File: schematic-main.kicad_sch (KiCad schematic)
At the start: 9 parts, among them J1 Conn_01x02_Pin, J2 Conn_01x02_Pin, J3 Conn_01x02_Pin, J4 Conn_01x02_Pin, P1 USB_C_Plug_USB2.0

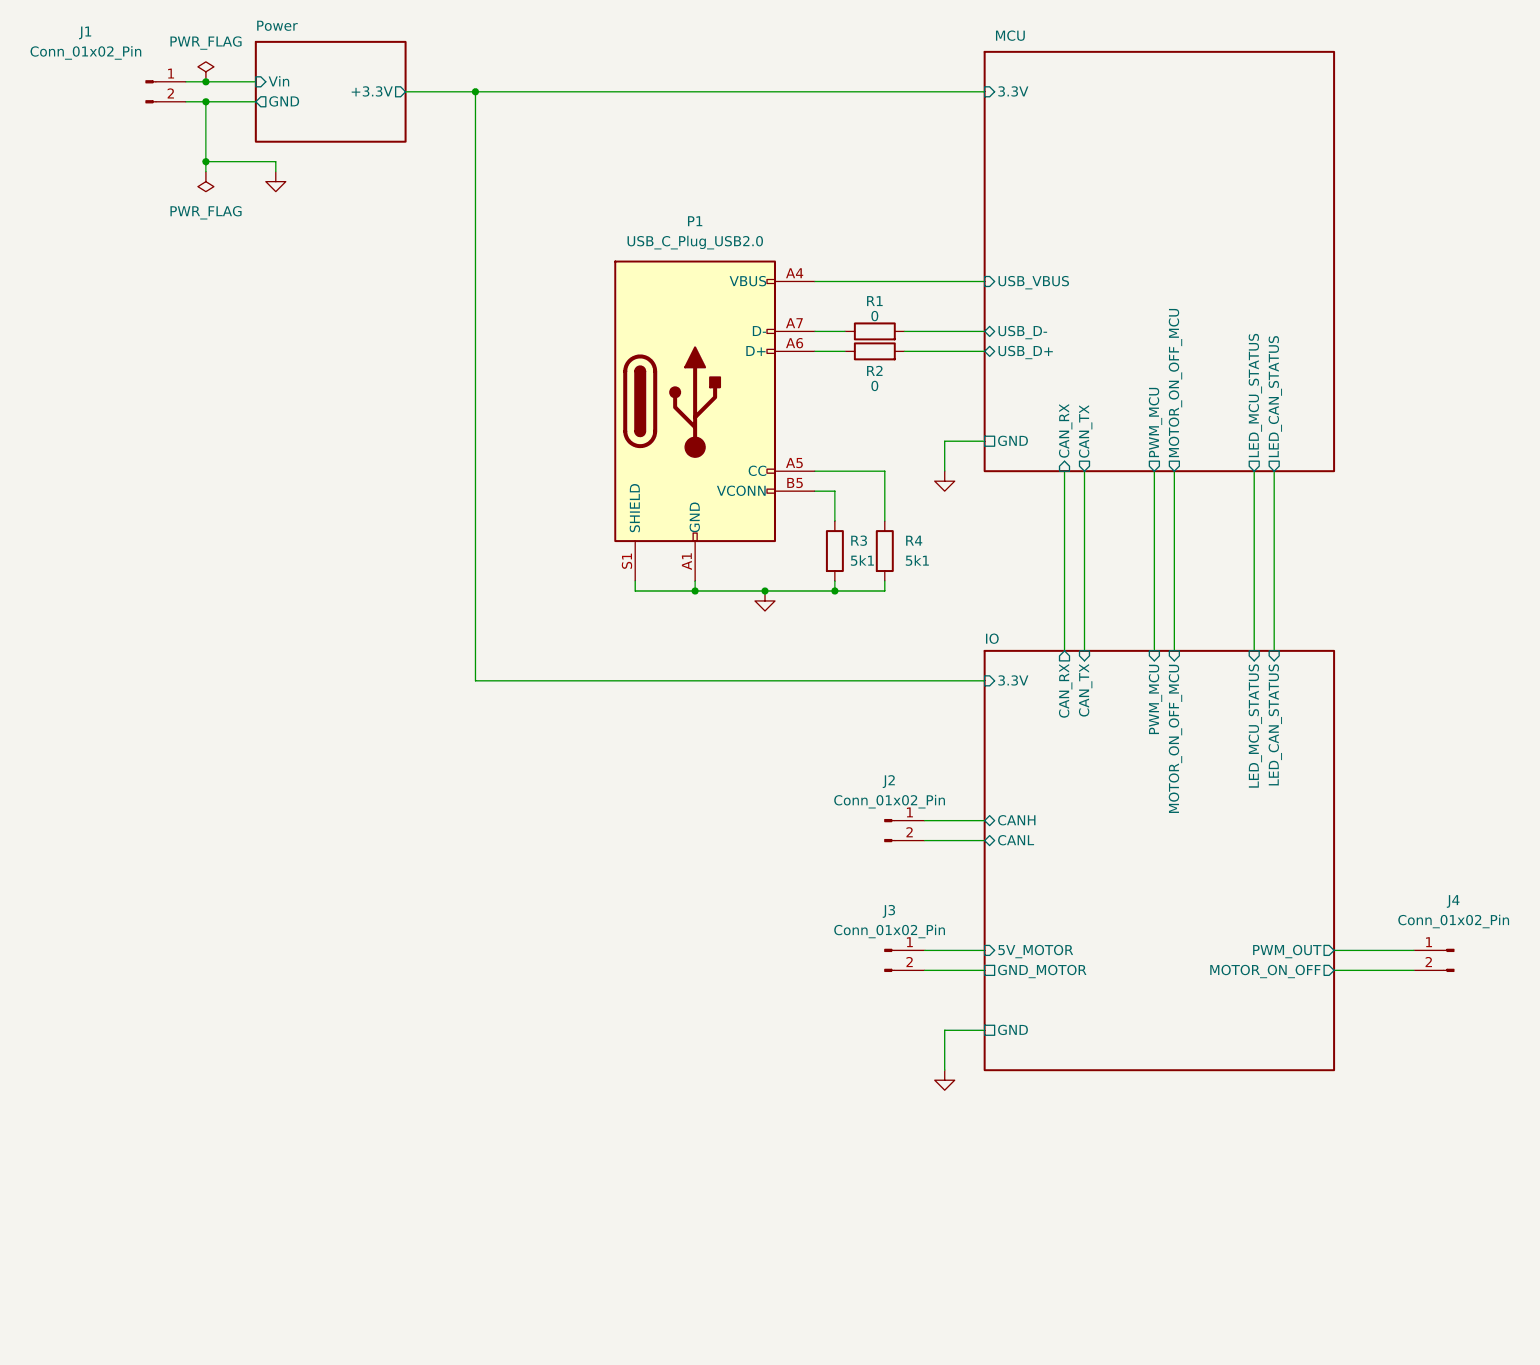
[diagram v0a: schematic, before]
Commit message: Add values for ideal diode circuit
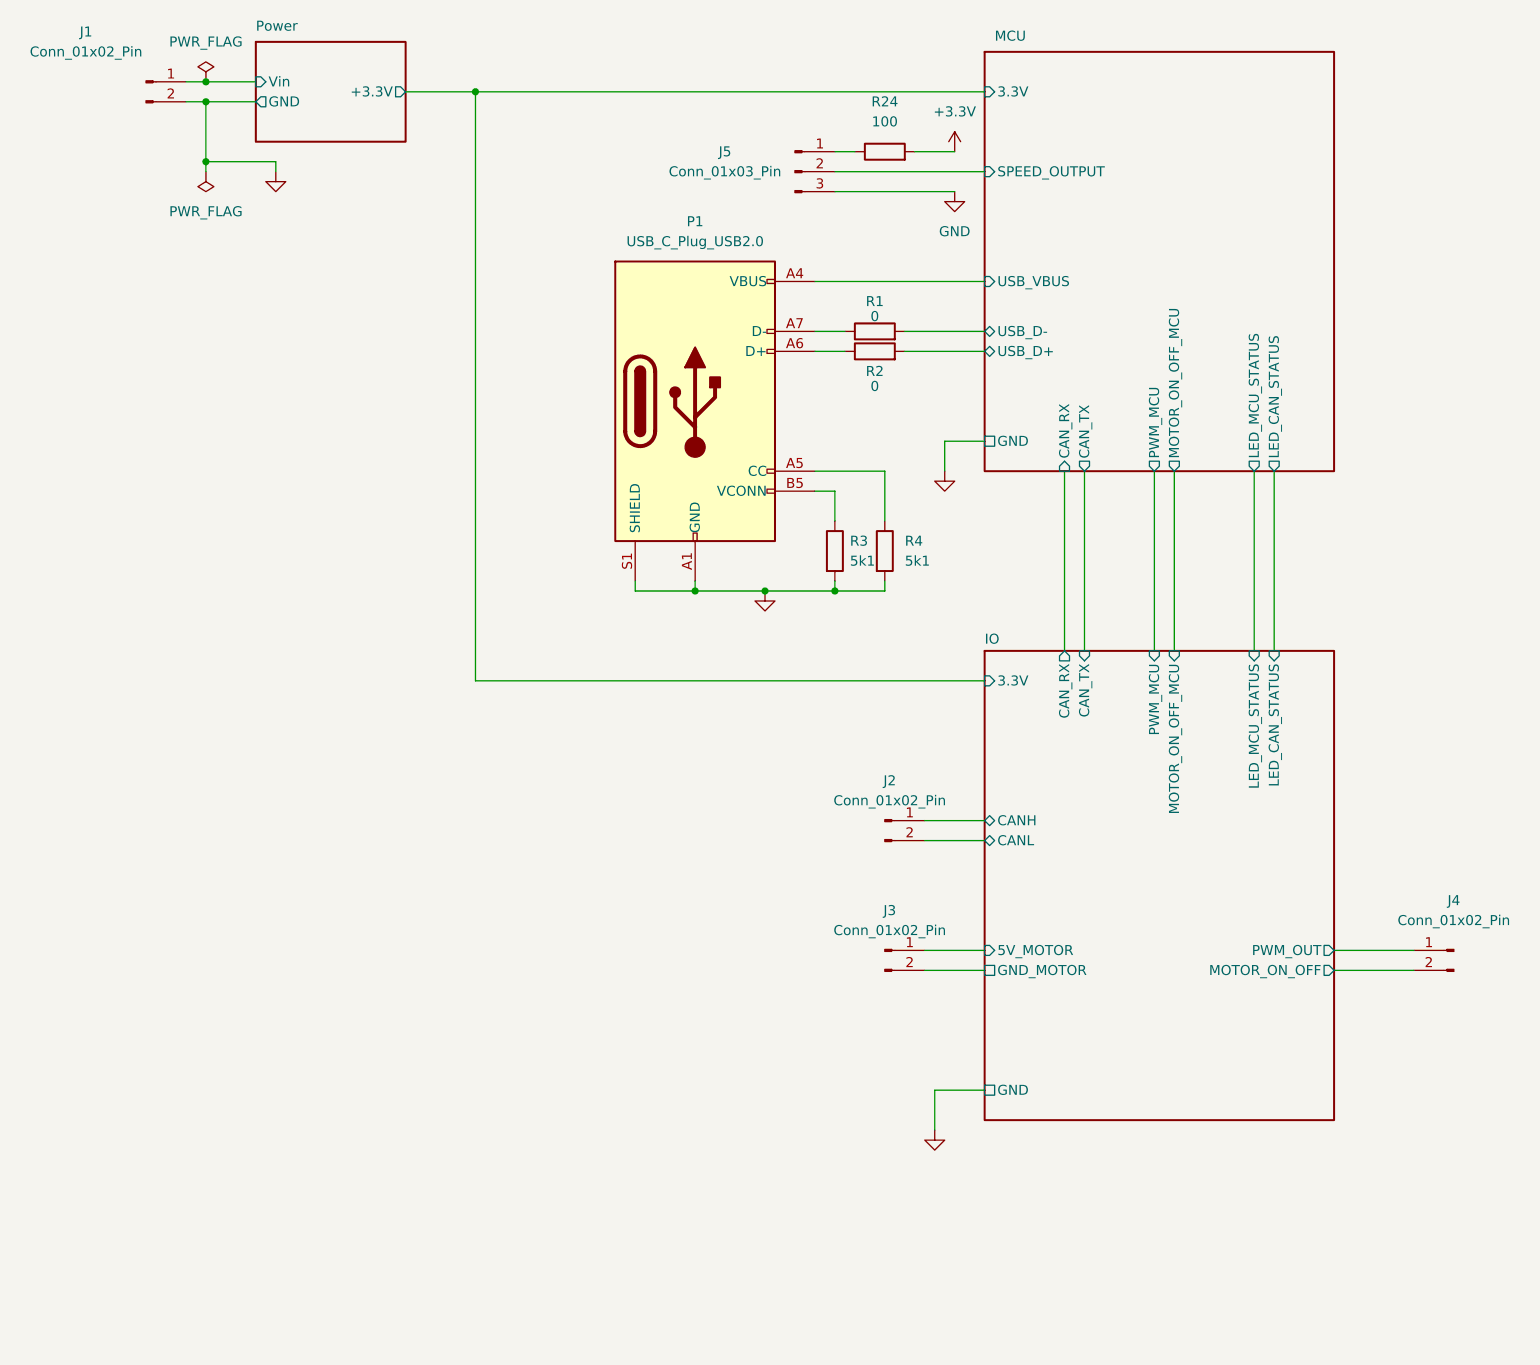
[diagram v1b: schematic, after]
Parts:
- added J5: Conn_01x03_Pin, symbol Connector:Conn_01x03_Pin
- added R24: 100, symbol Device:R
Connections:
- net GND: now also J5.3 (Pin_3)
- new net: J5.1 (Pin_1), R24.1
- new net +3.3V: R24.2
- new net MCU/SPEED_OUTPUT: J5.2 (Pin_2)
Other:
- sheet MCU ports: added SPEED_OUTPUT; removed none
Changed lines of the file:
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@@
+    (stroke (width 0) (type default))
+  )
+  (wire (pts (xy 115.57 40.64) (xy 118.11 40.64))
     (stroke (width 0) (type default))
   )
@@
     (stroke (width 0) (type default))
   )
+  (wire (pts (xy 115.57 45.72) (xy 130.81 45.72))
+    (stroke (width 0) (type default))
+  )
   (wire (pts (xy 156.21 81.28) (xy 156.21 104.14))
     (stroke (width 0) (type default))
@@
     (stroke (width 0) (type default))
   )
+  (wire (pts (xy 115.57 43.18) (xy 134.62 43.18))
+    (stroke (width 0) (type default))
+  )
+  (wire (pts (xy 125.73 40.64) (xy 130.81 40.64))
+    (stroke (width 0) (type default))
+  )
   (wire (pts (xy 69.85 33.02) (xy 69.85 107.95))
     (stroke (width 0) (type default))
@@
     (stroke (width 0) (type default))
   )
-  (wire (pts (xy 134.62 152.4) (xy 129.54 152.4))
+  (wire (pts (xy 134.62 160.02) (xy 128.27 160.02))
     (stroke (width 0) (type default))
   )
@@
     (stroke (width 0) (type default))
   )
-  (wire (pts (xy 129.54 152.4) (xy 129.54 157.48))
+  (wire (pts (xy 128.27 160.02) (xy 128.27 165.1))
     (stroke (width 0) (type default))
   )
@@
     (stroke (width 0) (type default))
   )
-  (symbol (lib_id "power:GND") (at 129.54 157.48 0) (unit 1)
-    (in_bom yes) (on_board yes) (dnp no) (fields_autoplaced)
-    (property "Reference" "#PWR04" (at 129.54 163.83 0)
-      (effects (font (size 1.27 1.27)) hide)
-    )
-    (property "Value" "GND" (at 129.54 162.56 0)
-      (effects (font (size 1.27 1.27)) hide)
-    )
-    (property "Footprint" "" (at 129.54 157.48 0)
-      (effects (font (size 1.27 1.27)) hide)
-    )
-    (property "Datasheet" "" (at 129.54 157.48 0)
+  (symbol (lib_id "power:GND") (at 128.27 165.1 0) (unit 1)
+    (in_bom yes) (on_board yes) (dnp no) (fields_autoplaced)
+    (property "Reference" "#PWR04" (at 128.27 171.45 0)
+      (effects (font (size 1.27 1.27)) hide)
+    )
+    (property "Value" "GND" (at 128.27 170.18 0)
+      (effects (font (size 1.27 1.27)) hide)
+    )
+    (property "Footprint" "" (at 128.27 165.1 0)
+      (effects (font (size 1.27 1.27)) hide)
+    )
+    (property "Datasheet" "" (at 128.27 165.1 0)
       (effects (font (size 1.27 1.27)) hide)
     )
@@
     )
   )
+  (symbol (lib_id "power:+3.3V") (at 130.81 40.64 0) (unit 1)
+    (in_bom yes) (on_board yes) (dnp no) (fields_autoplaced)
+    (property "Reference" "#PWR052" (at 130.81 44.45 0)
+      (effects (font (size 1.27 1.27)) hide)
+    )
+    (property "Value" "+3.3V" (at 130.81 35.56 0)
+      (effects (font (size 1.27 1.27)))
+    )
+    (property "Footprint" "" (at 130.81 40.64 0)
+      (effects (font (size 1.27 1.27)) hide)
+    )
+    (property "Datasheet" "" (at 130.81 40.64 0)
+      (effects (font (size 1.27 1.27)) hide)
+    )
+    (pin "1")
+    (instances
+      (project "schematic-main"
+        (path "/c9ad7189-d3b2-414a-9743-efd8e57cd755"
+          (reference "#PWR052") (unit 1)
+        )
+      )
+    )
+  )
   (symbol (lib_id "power:GND") (at 44.45 43.18 0) (unit 1)
     (in_bom yes) (on_board yes) (dnp no) (fields_autoplaced)
@@
       (effects (font (size 1.27 1.27)) hide)
     )
-    (pin "2")
-    (pin "1")
+    (pin "1")
+    (pin "2")
     (instances
       (project "schematic-main"
@@
     )
   )
+  (symbol (lib_id "Device:R") (at 121.92 40.64 90) (unit 1)
+    (in_bom yes) (on_board yes) (dnp no) (fields_autoplaced)
+    (property "Reference" "R24" (at 121.92 34.29 90)
+      (effects (font (size 1.27 1.27)))
+    )
+    (property "Value" "100" (at 121.92 36.83 90)
+      (effects (font (size 1.27 1.27)))
+    )
+    (property "Footprint" "" (at 121.92 42.418 90)
+      (effects (font (size 1.27 1.27)) hide)
+    )
+    (property "Datasheet" "~" (at 121.92 40.64 0)
+      (effects (font (size 1.27 1.27)) hide)
+    )
+    (pin "1")
+    (pin "2")
+    (instances
+      (project "schematic-main"
+        (path "/c9ad7189-d3b2-414a-9743-efd8e57cd755"
+          (reference "R24") (unit 1)
+        )
+      )
+    )
+  )
   (symbol (lib_id "power:GND") (at 129.54 81.28 0) (unit 1)
     (in_bom yes) (on_board yes) (dnp no) (fields_autoplaced)
@@
       (effects (font (size 1.27 1.27)) hide)
     )
-    (pin "2")
-    (pin "1")
+    (pin "1")
+    (pin "2")
     (instances
       (project "schematic-main"
@@
     )
   )
+  (symbol (lib_id "Connector:Conn_01x03_Pin") (at 110.49 43.18 0) (unit 1)
+    (in_bom yes) (on_board yes) (dnp no)
+    (property "Reference" "J5" (at 101.6 40.64 0)
+      (effects (font (size 1.27 1.27)))
+    )
+    (property "Value" "Conn_01x03_Pin" (at 101.6 43.18 0)
+      (effects (font (size 1.27 1.27)))
+    )
+    (property "Footprint" "" (at 110.49 43.18 0)
+      (effects (font (size 1.27 1.27)) hide)
+    )
+    (property "Datasheet" "~" (at 110.49 43.18 0)
+      (effects (font (size 1.27 1.27)) hide)
+    )
+    (pin "1")
+    (pin "2")
+    (pin "3")
+    (instances
+      (project "schematic-main"
+        (path "/c9ad7189-d3b2-414a-9743-efd8e57cd755"
+          (reference "J5") (unit 1)
+        )
+      )
+    )
+  )
   (symbol (lib_id "power:GND") (at 106.68 96.52 0) (unit 1)
     (in_bom yes) (on_board yes) (dnp no) (fields_autoplaced)
@@
       (effects (font (size 1.27 1.27)) hide)
     )
-    (pin "2")
-    (pin "1")
+    (pin "1")
+    (pin "2")
     (instances
       (project "schematic-main"
@@
       (effects (font (size 1.27 1.27)) hide)
     )
-    (pin "2")
-    (pin "1")
+    (pin "1")
+    (pin "2")
     (instances
       (project "schematic-main"
         (path "/c9ad7189-d3b2-414a-9743-efd8e57cd755"
           (reference "J4") (unit 1)
+        )
+      )
+    )
+  )
+  (symbol (lib_id "power:GND") (at 130.81 45.72 0) (unit 1)
+    (in_bom yes) (on_board yes) (dnp no) (fields_autoplaced)
+    (property "Reference" "#PWR053" (at 130.81 52.07 0)
+      (effects (font (size 1.27 1.27)) hide)
+    )
+    (property "Value" "GND" (at 130.81 50.8 0)
+      (effects (font (size 1.27 1.27)))
+    )
+    (property "Footprint" "" (at 130.81 45.72 0)
+      (effects (font (size 1.27 1.27)) hide)
+    )
+    (property "Datasheet" "" (at 130.81 45.72 0)
+      (effects (font (size 1.27 1.27)) hide)
+    )
+    (pin "1")
+    (instances
+      (project "schematic-main"
+        (path "/c9ad7189-d3b2-414a-9743-efd8e57cd755"
+          (reference "#PWR053") (unit 1)
         )
       )
@@
     )
   )
-  (sheet (at 134.62 104.14) (size 44.45 53.34) (fields_autoplaced)
+  (sheet (at 134.62 104.14) (size 44.45 59.69) (fields_autoplaced)
     (stroke (width 0.254) (type solid))
     (fill (color 255 255 154 1.0000))
@@
       (effects (font (size 1.27 1.27)) (justify left bottom))
     )
-    (property "Sheetfile" "schematc-io.kicad_sch" (at 134.62 158.1154 0)
+    (property "Sheetfile" "schematc-io.kicad_sch" (at 134.62 164.4654 0)
       (effects (font (size 1.27 1.27)) (justify left top) hide)
     )
@@
       (effects (font (size 1.27 1.27)) (justify left))
     )
-    (pin "GND" passive (at 134.62 152.4 180)
+    (pin "GND" passive (at 134.62 160.02 180)
       (effects (font (size 1.27 1.27)) (justify left))
     )
@@
       (effects (font (size 1.27 1.27)) (justify left))
     )
+    (pin "SPEED_OUTPUT" input (at 134.62 43.18 180)
+      (effects (font (size 1.27 1.27)) (justify left))
+    )

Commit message: Fix ERC checks related to hierarchical labels
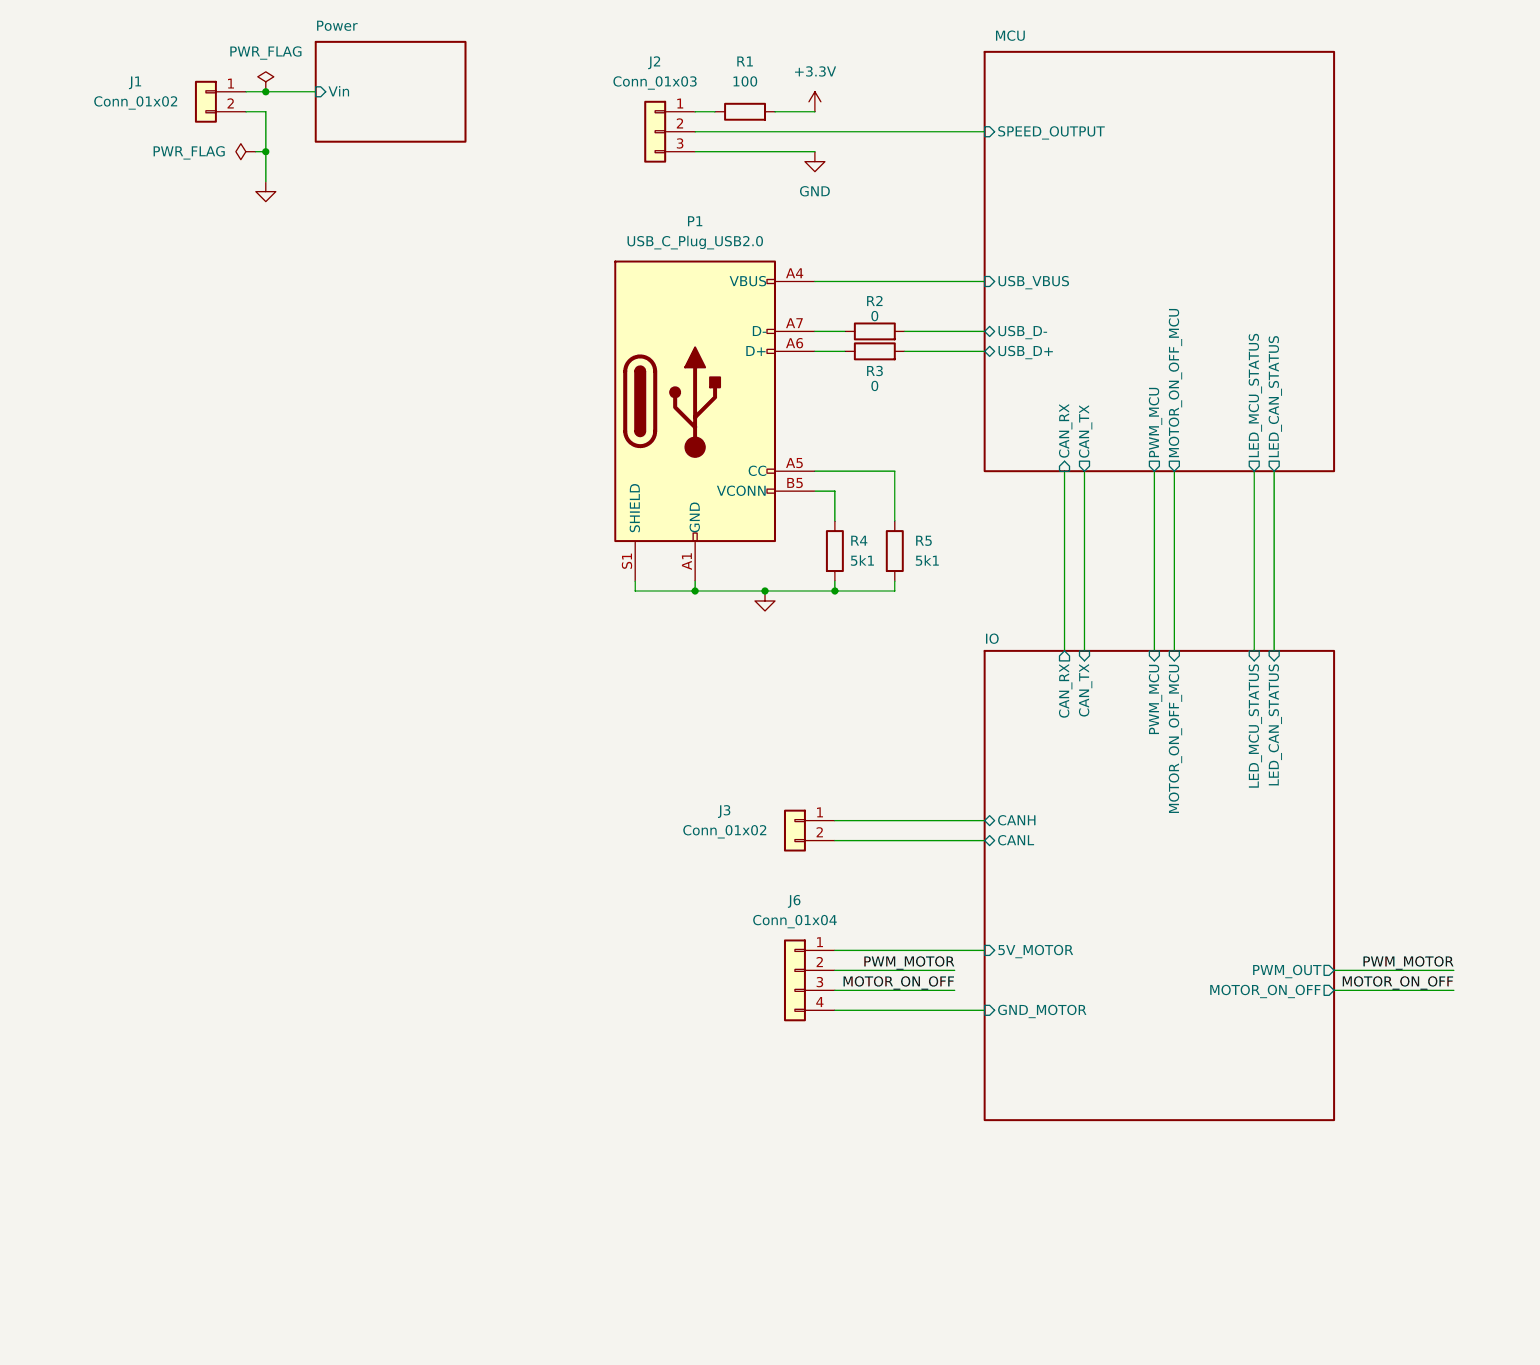
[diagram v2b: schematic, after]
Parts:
- removed J1, J2, J3, J4: Conn_01x02_Pin, symbol Connector:Conn_01x02_Pin
- removed J5: Conn_01x03_Pin, symbol Connector:Conn_01x03_Pin
- added J1, J3: Conn_01x02, symbol Connector_Generic:Conn_01x02
- added J2: Conn_01x03, symbol Connector_Generic:Conn_01x03
- added J6: Conn_01x04, symbol Connector_Generic:Conn_01x04
- renumbered R24 to R1, R1 to R2, R2 to R3, R3 to R4, R4 to R5
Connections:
- net GND: now also J1.2 (Pin_2), J2.3 (Pin_3)
- net IO/5V_MOTOR: now also J6.1 (Pin_1)
- net IO/CANH: now also J3.1 (Pin_1)
- net IO/CANL: now also J3.2 (Pin_2)
- net IO/GND_MOTOR: now also J6.4 (Pin_4)
- net MCU/SPEED_OUTPUT: now also J2.2 (Pin_2)
- net Power /Vin: now also J1.1 (Pin_1)
- net at R1.1: now also J2.1 (Pin_1)
- new net MOTOR_ON_OFF: J6.3 (Pin_3)
- new net PWM_MOTOR: J6.2 (Pin_2)
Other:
- sheet IO ports: added none; removed 3.3V, GND
- sheet MCU ports: added none; removed 3.3V, GND
- sheet Power  ports: added none; removed +3.3V, GND
- moved on the sheet: R1, R5
